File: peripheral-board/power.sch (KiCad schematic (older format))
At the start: 1 part

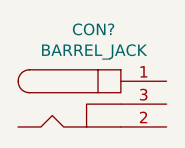
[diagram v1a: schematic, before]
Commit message: added button 3d model
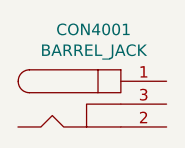
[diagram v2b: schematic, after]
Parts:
- gave numbers to parts that had none: 1
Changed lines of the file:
@@
 $EndDescr
 $Comp
-L BARREL_JACK CON?
+L BARREL_JACK CON4001
 U 1 1 581A8CF2
 P 2650 2700
-F 0 "CON?" H 2631 3025 50  0000 C CNN
+F 0 "CON4001" H 2631 3025 50  0000 C CNN
 F 1 "BARREL_JACK" H 2631 2934 50  0000 C CNN
-F 2 "" H 2650 2700 50  0000 C CNN
+F 2 "" H 2650 2700 50  0001 C CNN
 F 3 "" H 2650 2700 50  0000 C CNN
 	1    2650 2700

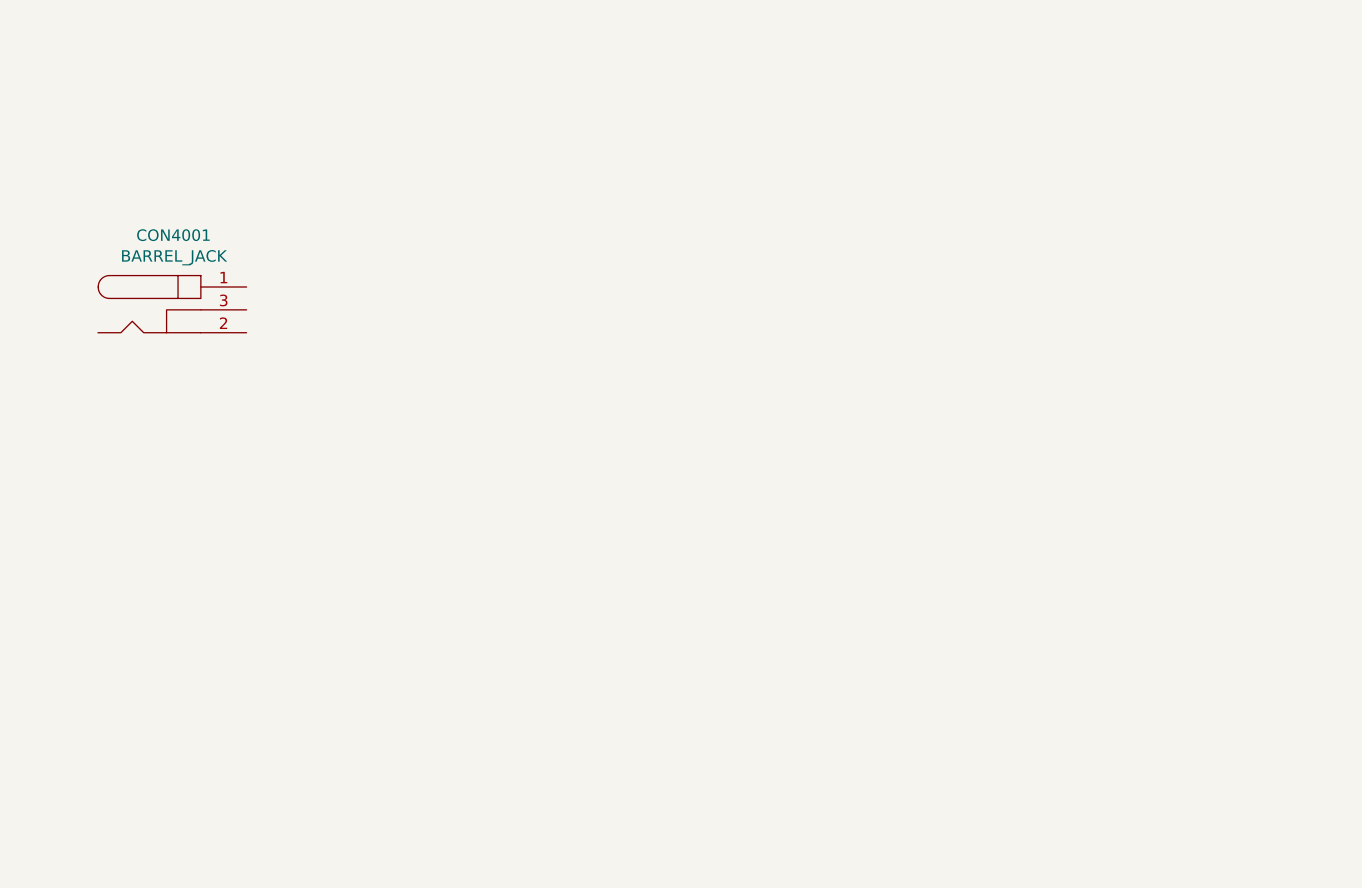
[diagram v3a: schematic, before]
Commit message: routed keyboard
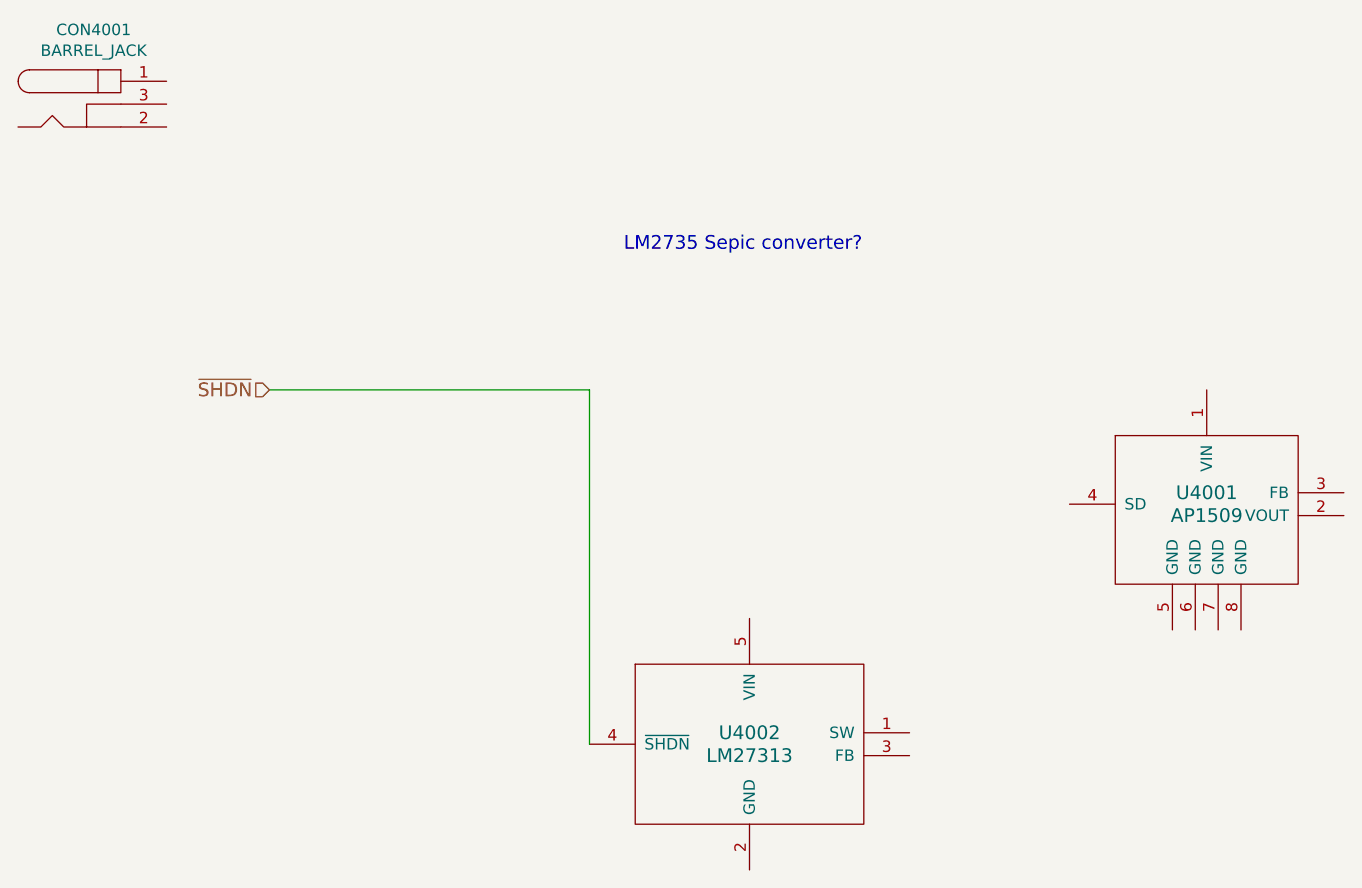
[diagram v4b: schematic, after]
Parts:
- added U4001: AP1509, symbol AP1509
- added U4002: LM27313, symbol LM27313
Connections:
- new net ~SHDN: U4002.4 (~SHDN)
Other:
- note added: "LM2735 Sepic converter?"
- moved on the sheet: CON4001
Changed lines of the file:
@@
 LIBS:amp
 LIBS:card-edge
+LIBS:switchmode
+LIBS:joystick
 LIBS:peripheral-board-cache
 EELAYER 25 0
@@
 L BARREL_JACK CON4001
 U 1 1 581A8CF2
-P 2650 2700
-F 0 "CON4001" H 2631 3025 50  0000 C CNN
-F 1 "BARREL_JACK" H 2631 2934 50  0000 C CNN
-F 2 "" H 2650 2700 50  0001 C CNN
-F 3 "" H 2650 2700 50  0000 C CNN
-	1    2650 2700
+P 2300 1800
+F 0 "CON4001" H 2281 2125 50  0000 C CNN
+F 1 "BARREL_JACK" H 2281 2034 50  0000 C CNN
+F 2 "" H 2300 1800 50  0001 C CNN
+F 3 "" H 2300 1800 50  0000 C CNN
+	1    2300 1800
 	1    0    0    -1
 $EndComp
+$Comp
+L AP1509 U4001
+U 1 1 58224E1C
+P 7150 3550
+F 0 "U4001" H 7150 3600 60  0000 C CNN
+F 1 "AP1509" H 7150 3500 60  0000 C CNN
+F 2 "" H 7150 3550 60  0001 C CNN
+F 3 "" H 7150 3550 60  0001 C CNN
+	1    7150 3550
+	1    0    0    -1
+$EndComp
+$Comp
+L LM27313 U4002
+U 1 1 582259B3
+P 5150 4600
+F 0 "U4002" H 5150 4650 60  0000 C CNN
+F 1 "LM27313" H 5150 4550 60  0000 C CNN
+F 2 "" H 5150 4600 60  0001 C CNN
+F 3 "" H 5150 4600 60  0001 C CNN
+	1    5150 4600
+	1    0    0    -1
+$EndComp
+Text Notes 4600 2450 0    60   ~ 0
+LM2735 Sepic converter?
+Text HLabel 3050 3050 0    60   Input ~ 0
+~SHDN
+Wire Wire Line
+	3050 3050 4450 3050
+Wire Wire Line
+	4450 3050 4450 4600
 $EndSCHEMATC

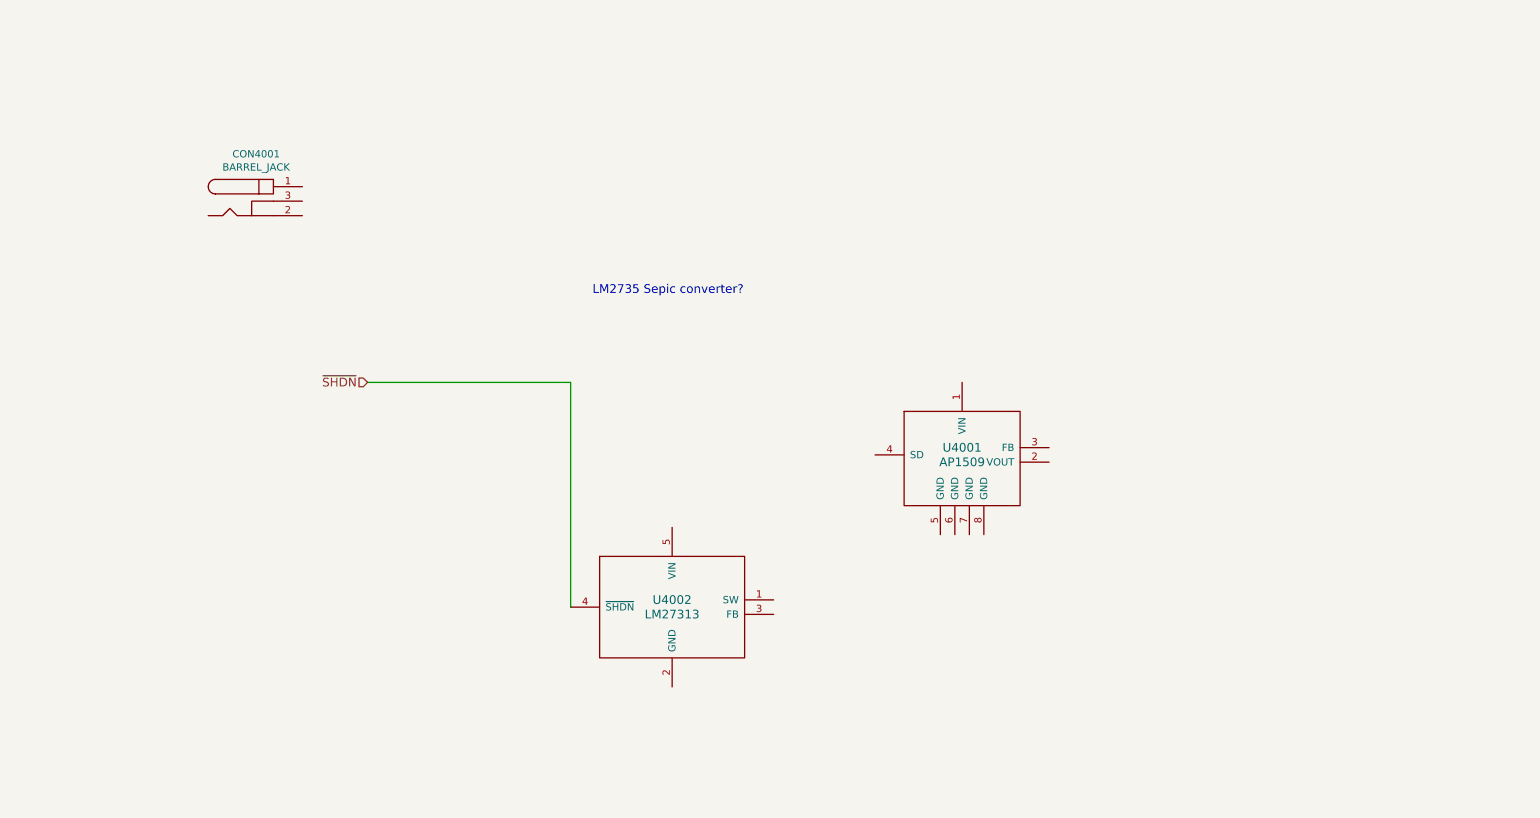
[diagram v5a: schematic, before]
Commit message: added battery charger schematic
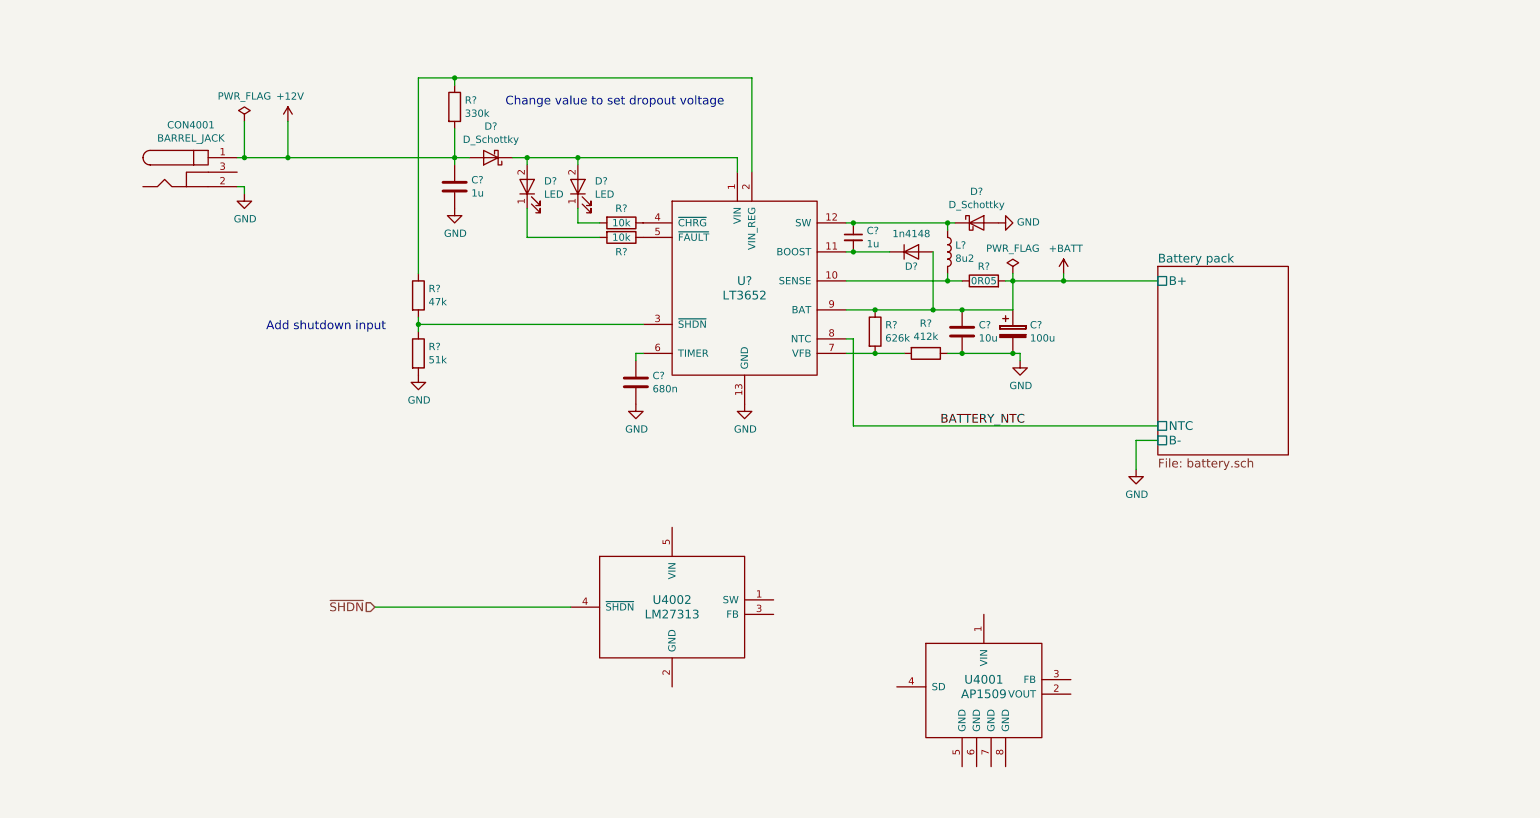
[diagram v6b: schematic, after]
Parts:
- added C?: 1u, symbol C_Small
- added C?: 10u, symbol C
- added C?: 100u, symbol CP
- added C?: 680n, symbol C
- added C?: 1u, symbol C
- added D?: 1n4148, symbol D
- added D? (x2): D_Schottky, symbol D_Schottky
- added D? (x2): LED, symbol LED
- added L?: 8u2, symbol L
- added R?: 626k, symbol R
- added R?: 412k, symbol R
- added R?: 0R05, symbol R
- added R? (x2): 10k, symbol R
- added R?: 47k, symbol R
- added R?: 330k, symbol R
- added R?: 51k, symbol R
- added U?: LT3652, symbol LT3652
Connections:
- net +12V: now reaches CON4001.1
- net +12V: now also C?.1, D?.2 (A), R?.2
- net GND: now reaches CON4001.2
- net GND: now also C?.2, C?.2, C?.2, C?.2, D?.2 (A), R?.1, R?.2, U?.13 (GND)
- new net: D?.1 (K), D?.2 (A), D?.2 (A), U?.1 (VIN)
- new net: L?.2, R?.1, U?.10 (SENSE)
- new net: C?.2, D?.1 (K), U?.11 (BOOST)
- new net: C?.1, D?.1 (K), L?.1, U?.12 (SW)
- new net: R?.1, R?.1, U?.2 (VIN_REG)
- new net: R?.1, R?.2, U?.3 (~SHDN)
- new net: R?.1, U?.4 (~CHRG)
- new net: R?.1, U?.5 (~FAULT)
- new net: C?.1, U?.6 (TIMER)
- new net: R?.2, R?.2, U?.7 (VFB)
- new net: D?.1 (K), R?.2 (x2)
- new net +BATT: C?.1, C?.1, D?.2 (A), R?.1, R?.2, U?.9 (BAT)
- new net BATTERY_NTC: U?.8 (NTC)
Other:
- note added: "Add shutdown input\n"
- note added: "Change value to set dropout voltage\n"
- note removed: "LM2735 Sepic converter?"
- moved on the sheet: CON4001, U4001

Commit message: added audio jack
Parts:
- added C4006: 2.2u, Capacitors_SMD:C_1206, symbol C
- added C4007, C4010: CP, symbol CP
- added C4008: 120p, Capacitors_SMD:C_0805, symbol C
- added C4009: 10u, Capacitors_SMD:C_1206, symbol C
- added D4001, D4008: RBE2VA20ATR, Diodes_SMD:D_TUMD2, symbol D_Schottky
- added D4007: NSR0530HT1G, Diodes_SMD:D_SOD-323, symbol D_Schottky
- added L4002: 10u, Choke_SMD:Choke_SMD_1206_Standard, symbol L
- added L4003: 47u, Choke_SMD:Choke_SMD_7.3x7.3_H4.5, symbol L
- added Q4001: Q_PMOS_DGS, symbol Q_PMOS_DGS
- added Q4002: Q_NMOS_DGS, symbol Q_NMOS_DGS
- added R4001: 10k, symbol R
- added R4010, R4011: R, symbol R
- added R4012: 270k, symbol R
- added R4013: 13.3k, symbol R
- C4001, C4002, C4003: renamed from C?; footprint (none) -> Capacitors_SMD:C_1206
- C4005: renamed from C?; footprint (none) -> Capacitors_SMD:C_0805
- CON4001: footprint (none) -> Connect:JACK_ALIM
- D4002, D4005: renamed from D?; value D_Schottky -> RBE2VA20ATR; footprint (none) -> Diodes_SMD:D_TUMD2
- D4006: renamed from D?; footprint (none) -> Diodes_SMD:D_MiniMELF_Standard
- L4001: renamed from L?; footprint (none) -> Choke_SMD:Choke_SMD_1206_Standard
- U4001: footprint (none) -> Housings_SOIC:SOIC-8_3.9x4.9mm_Pitch1.27mm
- U4002: footprint (none) -> TO_SOT_Packages_SMD:SOT-23-5
- U4003: renamed from U?; footprint (none) -> Housings_SSOP:MSOP-12-1EP_3x4mm_Pitch0.65mm
- gave numbers to parts that had none: 11
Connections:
- net +12V: now also D4001.2 (A), Q4001.2 (G), R4001.2
- net +BATT: now also Q4001.1 (D)
- net GND: now also U4001.5 (GND), U4001.6 (GND), U4001.7 (GND), U4001.8 (GND), U4002.2 (GND), C4006.2, C4007.2, C4009.2, C4010.2, D4008.2 (A), Q4002.3 (S), R4001.1, R4010.2, R4013.2
- net VCC: now reaches U4001.1 (VIN)
- net VCC: now also U4002.5 (VIN), C4007.1, D4001.1 (K), Q4001.3 (S)
- net at U4001.2 (VOUT): now also D4008.1 (K), L4003.1
- net +3V3: now reaches U4001.3 (FB)
- net +3V3: now also C4010.1, L4003.2
- net SHDN: now reaches U4001.4 (SD)
- net SHDN: now also Q4002.2 (G), R4010.1
- net at U4002.1 (SW): now also D4007.2 (A), L4002.2
- net at U4002.3 (FB): now also C4008.2, R4012.1, R4013.1
- net ~SHDN: no longer names the net of U4002.4 (~SHDN)
- net ~SHDN: now also Q4002.1 (D), R4011.2
- new net: C4006.1, L4002.1
- new net +24V: C4008.1, C4009.1, D4007.1 (K), R4012.2
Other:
- moved on the sheet: C4001, C4002, C4003, C4004, C4005, CON4001, D4002, D4003, D4004, D4005, D4006, L4001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
